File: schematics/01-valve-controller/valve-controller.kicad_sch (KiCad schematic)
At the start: 35 parts, among them J101 5V, J102 12V, J103 24V, J105 SWD, J106 SERIAL, U101 MAX604, U102 STM32F405RGT6, U103 MAX14787E, Y101 26M

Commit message: Added servo controller
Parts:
- added R103, R104: 4.7KΩ, symbol Device:R
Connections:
- new net +3V3: R103.1, R104.1
- new net SCL: R104.2
- new net SDA: R103.2
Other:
- added sheet Servo Controller (servo_controller.kicad_sch)
- note removed: "TODO: Add servo driver"

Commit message: Removed driver mosfets
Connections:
- net +3V3 is gone; now on net 1v8: R103.1, R104.1
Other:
- sheet Servo Controller ports: added SERVO_PWM_0, SERVO_PWM_1, SERVO_PWM_2, SERVO_PWM_3, SERVO_PWM_4; removed SERVO_GND_0, SERVO_GND_1, SERVO_GND_2, SERVO_GND_3, SERVO_GND_4
- note added: "Servo Controller"

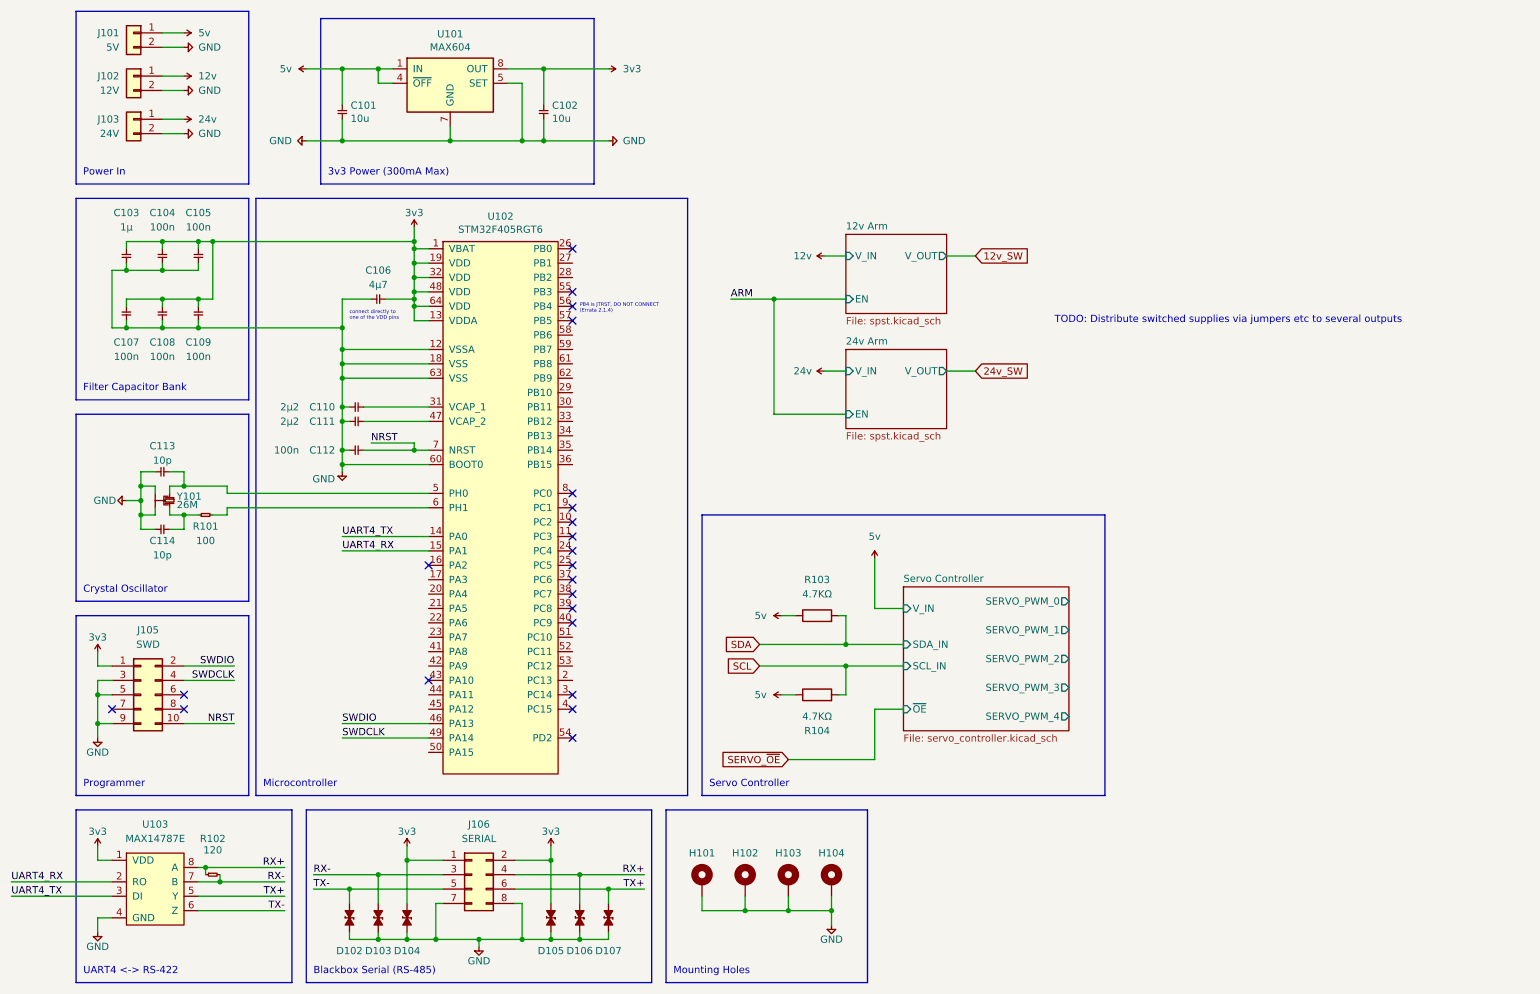
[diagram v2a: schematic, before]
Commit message: DC output switching, GPIO expander
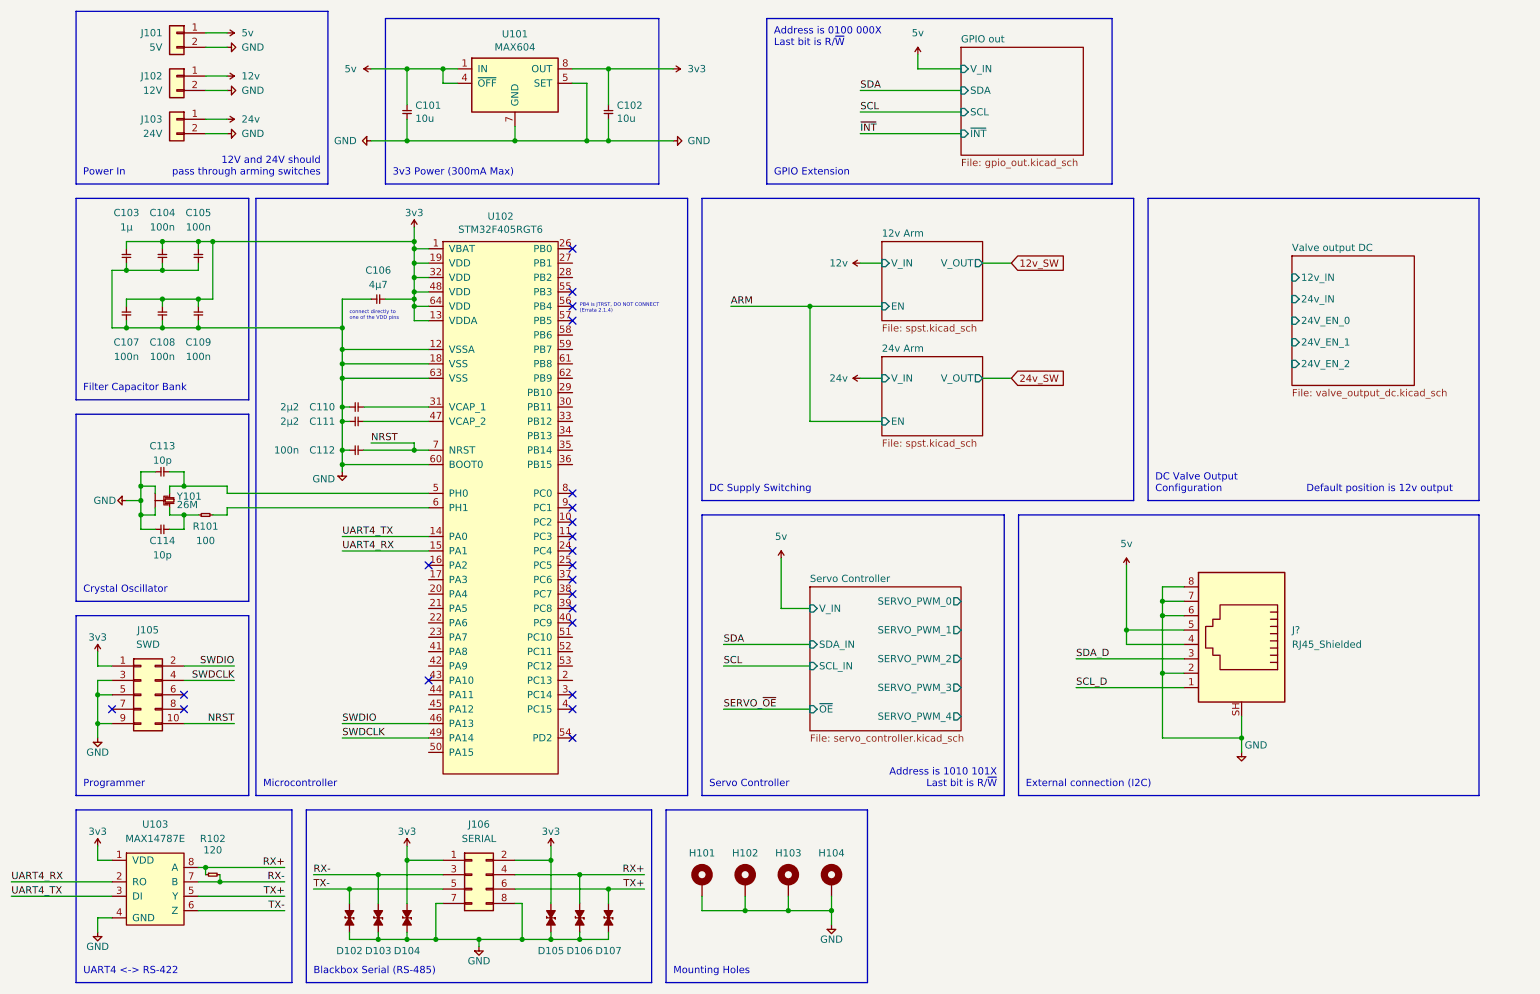
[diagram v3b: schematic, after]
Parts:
- removed R103, R104: 4.7KΩ, symbol Device:R
- added J?: RJ45_Shielded, symbol Connector:RJ45_Shielded
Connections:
- net 1v8: now also J?.4, J?.5
- net GND: now also J?.2, J?.6, J?.7, J?.8, J?.SH
- new net SCL_D: J?.1
- new net SDA_D: J?.3
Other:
- added sheet GPIO out (gpio_out.kicad_sch)
- added sheet Valve output DC (valve_output_dc.kicad_sch)
- note added: "12V and 24V should pass through arming switches"
- note added: "Address is 0100 000X Last bit is R/~{W}"
- note added: "Address is 1010 101X Last bit is R/~{W}"
- note added: "DC Supply Switching"
- note added: "DC Valve Output Configuration"
- note added: "Default position is 12v output"
- note added: "External connection (I2C)"
- note added: "GPIO Extension"
- note removed: "TODO: Distribute switched supplies via jumpers etc to several outputs"
- moved on the sheet: C101, C102, J101, J102, J103, U101
